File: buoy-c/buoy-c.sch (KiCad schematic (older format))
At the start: 36 parts

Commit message: Added regulator, stepup, accelerometer, battery charger, servo and battery measurement
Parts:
- removed D? (x2): RED-CLEAR, LED_SMD:LED_0805_2012Metric, symbol LED-RED-CLEAR-0805:RED-CLEAR
- removed Q? (x2): MMBT2222LT1G, Package_TO_SOT_SMD:SOT-23, symbol NPN-30V-600~mA:MMBT2222LT1G
- removed U?: TP4056, symbol TP4056:TP4056
- added C1: 47uF, Capacitor_SMD:C_0805_2012Metric, symbol C-47uF-0805:47uF
- added C13: 10uF, Capacitor_SMD:C_0805_2012Metric, symbol C-10uF-0805:10uF
- added C14: 100nF, Capacitor_SMD:C_0805_2012Metric, symbol C-100nF-0805:100nF
- added C15: 1uF, Capacitor_SMD:C_0805_2012Metric, symbol C-1uF-0805:1uF
- added C17: 2.2uF, Capacitor_SMD:C_0805_2012Metric, symbol C-2.2uF-0805:2.2uF
- added C19: 220uF, C-2917-7343-Metric:C-2917-7343-Metric, symbol C-220uF-2917:220uF
- added C4: 12pF, Capacitor_SMD:C_0805_2012Metric, symbol C-12pF-0805:12pF
- added C5: 680pF, Capacitor_SMD:C_0805_2012Metric, symbol C-680pF-0805:680pF
- added C6: 47pF, Capacitor_SMD:C_0805_2012Metric, symbol C-47pF-0805:47pF
- added C8: 100uF, Capacitor_SMD:C_1210_3225Metric, symbol C-100uF-1210:100uF
- added D1: ORANGE-CLEAR, LED_SMD:LED_0805_2012Metric, symbol LED-ORANGE-CLEAR-0805:ORANGE-CLEAR
- added D2: GREEN-CLEAR, LED_SMD:LED_0805_2012Metric, symbol LED-GREEN-CLEAR-0805:GREEN-CLEAR
- added J3, J7: TERM-BLK-2P, TerminalBlock:TerminalBlock_bornier-2_P5.08mm, symbol TERMINAL-BLOCK-2P-508:TERM-BLK-2P
- added J5: BH-18650-PC, Battery:BatteryHolder_MPD_BH-18650-PC2, symbol BH-18650-PC:BH-18650-PC
- added J6, J8: Conn_01x03_Male, Connector_PinHeader_2.54mm:PinHeader_1x03_P2.54mm_Vertical, symbol Connector:Conn_01x03_Male
- added L1: 104CDMCCDS-2R2MC, L-11.5x10.3x4:L-11.5x10.3x4, symbol L-2.2uH-11.5x10.3x4:104CDMCCDS-2R2MC
- added L2: 5.5uH, L-10.5x10.2x5:L-10.5x10.2x5, symbol L-5.5uH-10.5x10.2x5:5.5uH
- added Q1, Q2, Q3: MMBT2222LT1G, Package_TO_SOT_SMD:SOT-23, symbol NPN-30V-600mA:MMBT2222LT1G
- added R1, R26: 1M, Resistor_SMD:R_0805_2012Metric, symbol R-1M-0805:1M
- added R11: 6.49K, Resistor_SMD:R_0805_2012Metric, symbol R-6.49K-0805:6.49K
- added R14: 5.1k, Resistor_SMD:R_0805_2012Metric, symbol R-5.1k-0805:5.1k
- added R15, R16, R18, R25: 10K, Resistor_SMD:R_0805_2012Metric, symbol R-10K-0805:10K
- added R17: 1K, Resistor_SMD:R_0805_2012Metric, symbol R-1K-0805:1K
- added R19: 1.8M, Resistor_SMD:R_0805_2012Metric, symbol R-1.8M-0805:1.8M
- added R2: 90.9K, Resistor_SMD:R_0805_2012Metric, symbol R-90.9K-0805:90.9K
- added R20: 390K, Resistor_SMD:R_0805_2012Metric, symbol R-390K-0805:390K
- added R21: 806K, Capacitor_SMD:C_0805_2012Metric, symbol R-806K-0805:806K
- added R22: 2M, Capacitor_SMD:C_0805_2012Metric, symbol R-2M-0805:2M
- added R27: 180K, Resistor_SMD:R_0805_2012Metric, symbol R-180K-0805:180K
- added R7: 49.9K, Resistor_SMD:R_0805_2012Metric, symbol R-49.9K-0805:49.9K
- added R8: 825K, Resistor_SMD:R_0805_2012Metric, symbol R-825K-0805:825K
- added R9: 182K, Resistor_SMD:R_0805_2012Metric, symbol R-182K-0805:182K
- added U2: LTC3113EFE#TRPBF, Package_SO:HTSSOP-20-1EP_4.4x6.5mm_P0.65mm_EP3.4x6.5mm_Mask2.75x3.43mm_ThermalVias_HandSolder, symbol LTC3113EFE#TRPBF:LTC3113EFE#TRPBF
- added U3: TP4056, ESOP-8:ESOP-8, symbol TP4056:TP4056
- added U6: TPS61030PWPR, Package_SO:HTSSOP-16-1EP_4.4x5mm_P0.65mm_EP3.4x5mm_Mask3x3mm_ThermalVias, symbol TPS61030PWPR:TPS61030PWPR
- added U8: DS3231M+TRL, Package_SO:SOIC-16W_7.5x10.3mm_P1.27mm, symbol DS3231M+TRL:DS3231M+TRL
- added U9: ADXL343-EVAL, ADXL343-EVAL:ADXL343-EVAL, symbol ADXL343-EVAL:ADXL343-EVAL
- gave numbers to parts that had none: 31
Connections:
- net labels added: +BATT, 3V3_FTDI, BAT-CR2032, BATT_LEVEL, EN_STEPUP, INT_RTC, PWM_SERVO, RST_RTC, SCL, SDA, VDD
- wire segments 175 -> 346
- no-connect marks 43 -> 59
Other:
- note added: "2-3 Connects VDD to the Battery\n2-1 Connects VDD to 3V3"
- note added: "3V3"
- note added: "5V STEPUP"
- note added: "ACCELEROMETER"
- note added: "BATT"
- note added: "BATTERY CHARGER"
- note added: "BATT\nLEVEL"
- note added: "ESP32"
- note added: "Qi Wireless \nCharger"
- note added: "RTC"
- note added: "SEPIC Regulator 3V3"
- note added: "SERVO"
- note added: "VDD"
- note added: "VDD Selector"
- moved on the sheet: C10, C11, C12, C16, C18, C2, C3, C7, C9, D3, FB1, FB2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

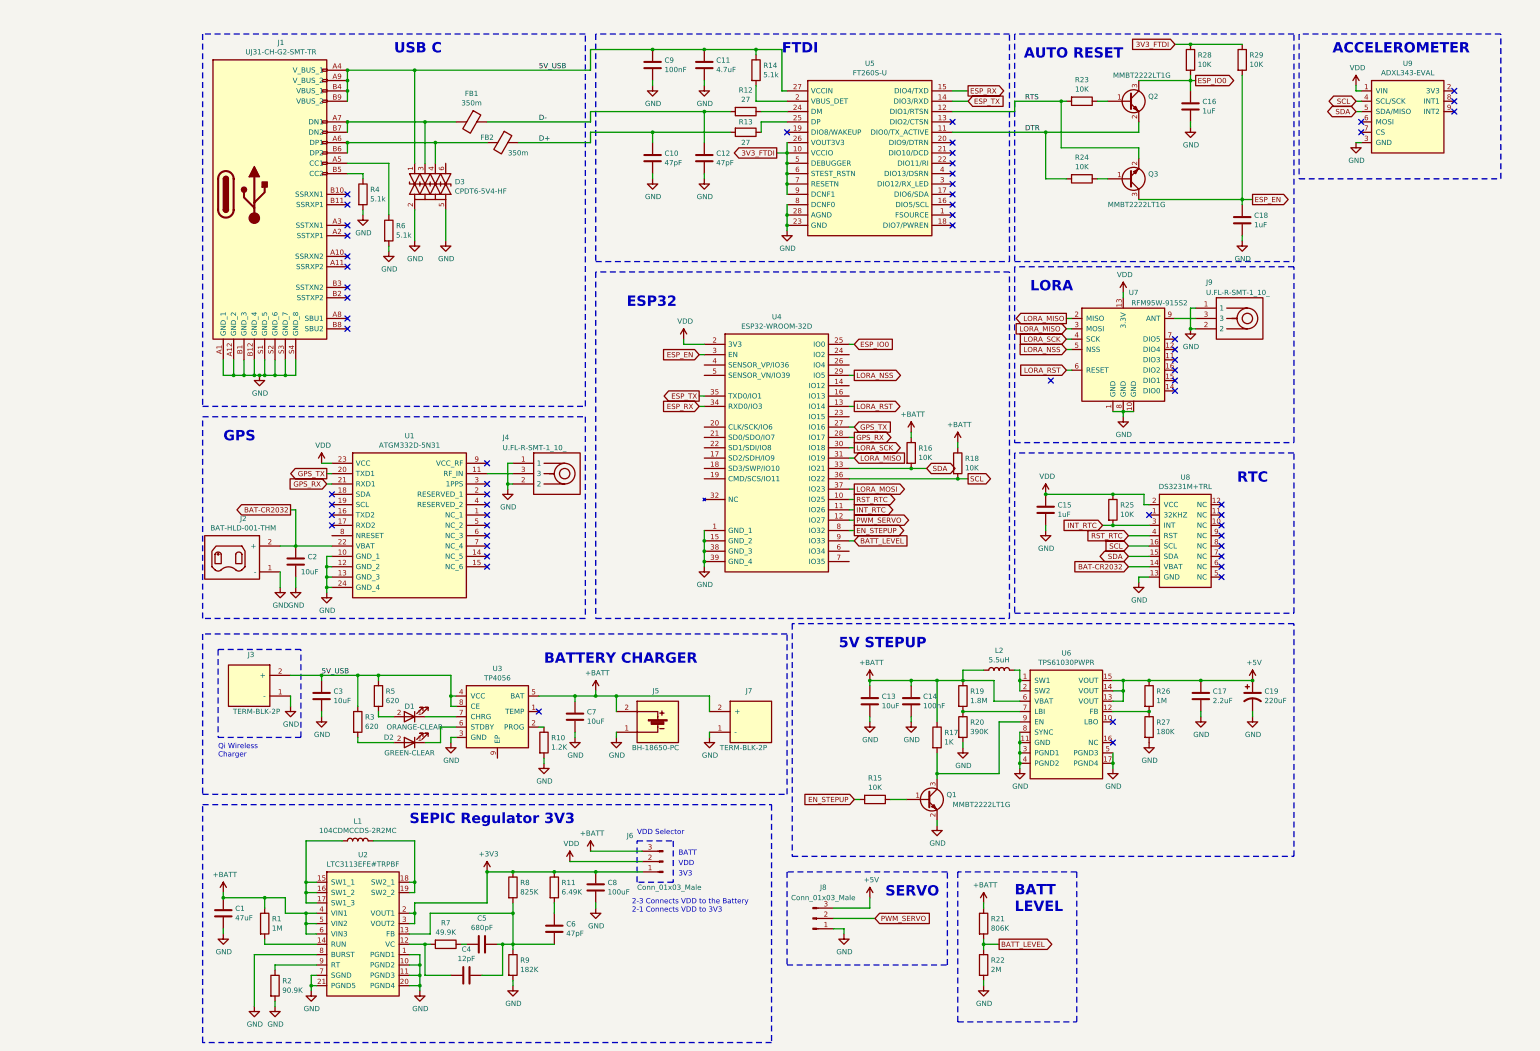
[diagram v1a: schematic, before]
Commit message: Defined board shape, placed components in the PCB
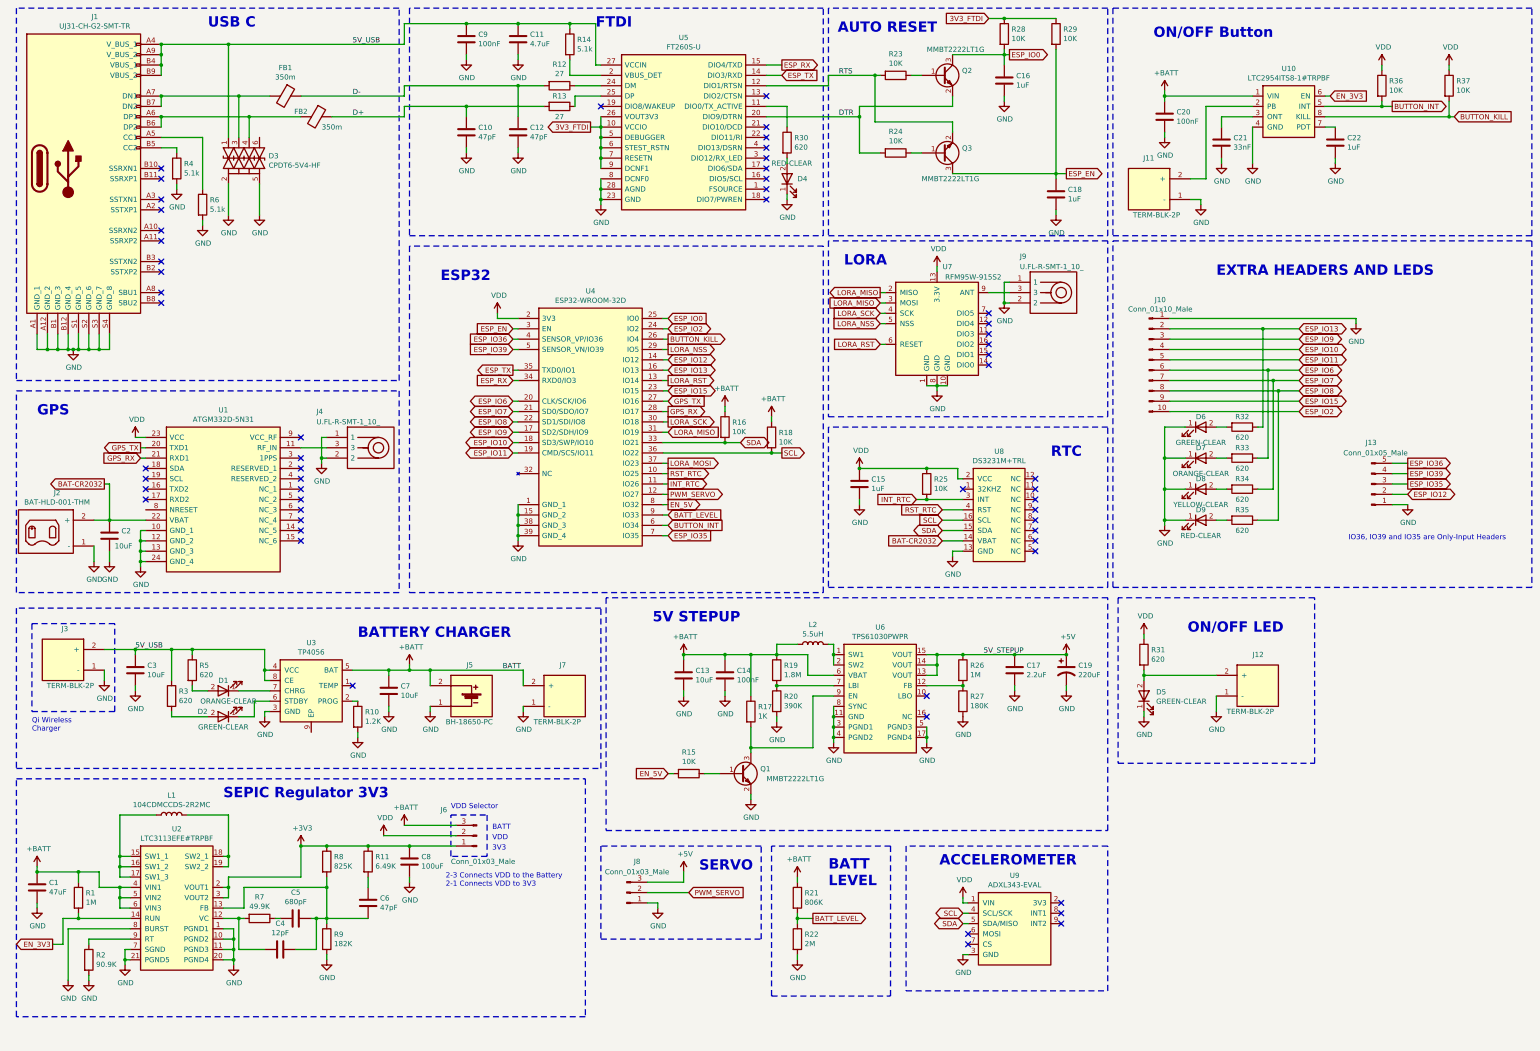
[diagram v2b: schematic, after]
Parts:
- added C20: 100nF, Capacitor_SMD:C_0805_2012Metric, symbol C-100nF-0805:100nF
- added C21: 33nF, Capacitor_SMD:C_0805_2012Metric, symbol C-33nF-0805:33nF
- added C22: 1uF, Capacitor_SMD:C_0805_2012Metric, symbol C-1uF-0805:1uF
- added D4, D9: RED-CLEAR, LED_SMD:LED_0805_2012Metric, symbol LED-RED-CLEAR-0805:RED-CLEAR
- added D5, D6: GREEN-CLEAR, LED_SMD:LED_0805_2012Metric, symbol LED-GREEN-CLEAR-0805:GREEN-CLEAR
- added D7: ORANGE-CLEAR, LED_SMD:LED_0805_2012Metric, symbol LED-ORANGE-CLEAR-0805:ORANGE-CLEAR
- added D8: YELLOW-CLEAR, LED_SMD:LED_0805_2012Metric, symbol LED-YELLOW-CLEAR-0805:YELLOW-CLEAR
- added J10: Conn_01x10_Male, Connector_PinHeader_2.54mm:PinHeader_1x10_P2.54mm_Vertical, symbol Connector:Conn_01x10_Male
- added J11, J12: TERM-BLK-2P, TerminalBlock:TerminalBlock_bornier-2_P5.08mm, symbol TERMINAL-BLOCK-2P-508:TERM-BLK-2P
- added J13: Conn_01x05_Male, Connector_PinHeader_2.54mm:PinHeader_1x05_P2.54mm_Vertical, symbol Connector:Conn_01x05_Male
- added R30, R31, R32, R33, R34, R35: 620, Resistor_SMD:R_0805_2012Metric, symbol R-620-0805:620
- added R36, R37: 10K, Resistor_SMD:R_0805_2012Metric, symbol R-10K-0805:10K
- added U10: LTC2954ITS8-1#TRPBF, Package_TO_SOT_SMD:TSOT-23-8_HandSoldering, symbol LTC2954ITS8-1#TRPBF:LTC2954ITS8-1#TRPBF
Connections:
- net +BATT: now also C20.1, U10.1 (VIN)
- net DTR: now also U5.20 (DIO9/DTRN); no longer U5.11 (DIO0/TX_ACTIVE)
- net GND: now also C20.2, C21.2, C22.2, D4.1 (K), D5.1 (K), D6.1 (K), D7.1 (K), D8.1 (K), D9.1 (K), J10.1 (Pin_1), J11.1 (-), J12.1 (-), J13.1 (Pin_1), U10.4 (GND)
- net VDD: now also R31.1, R36.1, R37.1
- net EN_3V3: now reaches R1.2, U2.14 (RUN)
- net EN_3V3: now also U10.6 (EN)
- net ESP_IO12: now reaches U4.14 (IO12)
- net ESP_IO12: now also J13.2 (Pin_2)
- net ESP_IO13: now reaches U4.16 (IO13)
- net ESP_IO13: now also J10.2 (Pin_2), R32.1
- net ESP_IO9: now reaches U4.17 (SD2/SDH/IO9)
- net ESP_IO9: now also J10.3 (Pin_3)
- net ESP_IO10: now reaches U4.18 (SD3/SWP/IO10)
- net ESP_IO10: now also J10.4 (Pin_4)
- net ESP_IO11: now reaches U4.19 (CMD/SCS/IO11)
- net ESP_IO11: now also J10.5 (Pin_5)
- net ESP_IO6: now reaches U4.20 (CLK/SCK/IO6)
- net ESP_IO6: now also J10.6 (Pin_6), R33.1
- net ESP_IO7: now reaches U4.21 (SD0/SDO/IO7)
- net ESP_IO7: now also J10.7 (Pin_7), R34.1
- net ESP_IO8: now reaches U4.22 (SD1/SDI/IO8)
- net ESP_IO8: now also J10.8 (Pin_8), R35.1
- net ESP_IO15: now reaches U4.23 (IO15)
- net ESP_IO15: now also J10.9 (Pin_9)
- net ESP_IO2: now reaches U4.24 (IO2)
- net ESP_IO2: now also J10.10 (Pin_10)
- net BUTTON_KILL: now reaches U4.26 (IO4)
- net BUTTON_KILL: now also R37.2, U10.8 (KILL)
- net ESP_IO36: now reaches U4.4 (SENSOR_VP/IO36)
- net ESP_IO36: now also J13.5 (Pin_5)
- net ESP_IO39: now reaches U4.5 (SENSOR_VN/IO39)
- net ESP_IO39: now also J13.4 (Pin_4)
- net BUTTON_INT: now reaches U4.6 (IO34)
- net BUTTON_INT: now also R36.2, U10.5 (INT)
- net ESP_IO35: now reaches U4.7 (IO35)
- net ESP_IO35: now also J13.3 (Pin_3)
- net EN_STEPUP renamed EN_5V
- new net: R30.1, U5.11 (DIO0/TX_ACTIVE)
- new net: J11.2 (+), U10.2 (PB)
- new net: C21.1, U10.3 (ONT)
- new net: C22.1, U10.7 (PDT)
- new net: D5.2 (A), J12.2 (+), R31.2
- new net: D4.2 (A), R30.2
- new net: D6.2 (A), R32.2
- new net: D7.2 (A), R33.2
- new net: D8.2 (A), R34.2
- new net: D9.2 (A), R35.2
- no-connect marks 59 -> 57
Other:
- note added: "EXTRA HEADERS AND LEDS"
- note added: "IO36, IO39 and IO35 are Only-Input Headers"
- note added: "ON/OFF Button"
- note added: "ON/OFF LED"
- moved on the sheet: C1, C10, C11, C12, C13, C14, C15, C16, C17, C18, C19, C2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
